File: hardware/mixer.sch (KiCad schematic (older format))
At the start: 31 parts, among them U26 5400BL15B050E, U27 5400BL15B050E, U28 5400BL15B050E, U29 ADL5802

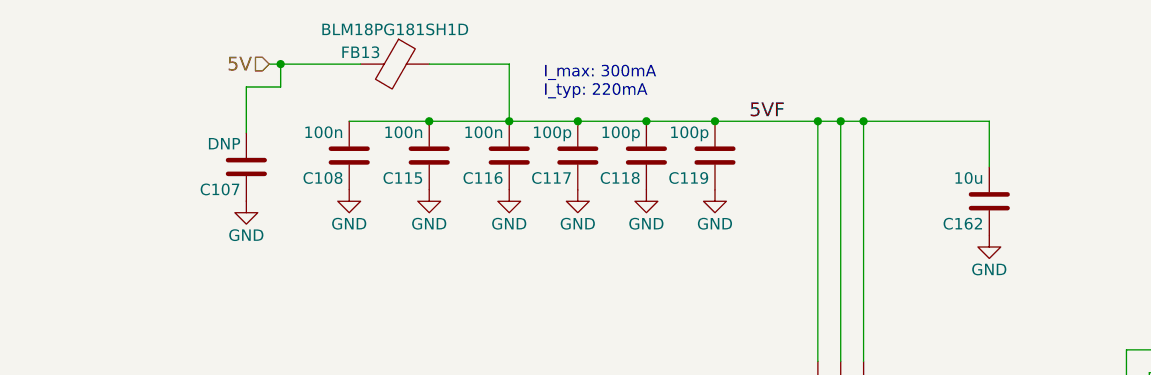
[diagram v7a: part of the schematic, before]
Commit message: Fixed ERC errors.
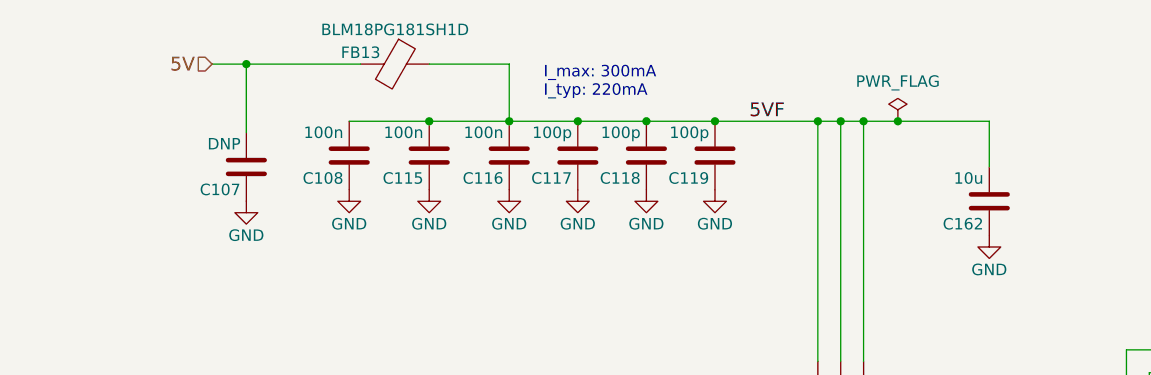
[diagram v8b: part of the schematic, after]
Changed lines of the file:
@@
 Text HLabel 8600 3450 2    60   Output ~ 0
 IF1-
-Text HLabel 3100 2200 0    60   Input ~ 0
-5V
 $Comp
 L fmcw-rescue:ADL5802-fmcw3-rescue U?
@@
 	1    0    0    -1
 $EndComp
-Wire Wire Line
-	3000 2500 3000 2300
-Wire Wire Line
-	3000 2300 3150 2300
-Wire Wire Line
-	3150 2300 3150 2200
-Wire Wire Line
-	3100 2200 3150 2200
-Connection ~ 3150 2200
 Connection ~ 4750 2450
 Text Label 5200 2450 0    60   ~ 0
@@
 	4750 2450 5050 2450
 Wire Wire Line
-	5700 2450 6250 2450
+	5700 2450 5850 2450
 Wire Wire Line
 	5250 5300 5350 5300
-Wire Wire Line
-	3150 2200 3500 2200
 Wire Wire Line
 	3800 2200 4150 2200
@@
 Wire Wire Line
 	950  4050 2100 4050
+Wire Wire Line
+	2850 2200 3000 2200
+Wire Wire Line
+	3000 2200 3000 2500
+Connection ~ 3000 2200
+Wire Wire Line
+	3000 2200 3500 2200
+$Comp
+L power:PWR_FLAG #FLG0110
+U 1 1 5CDA3D12
+P 5850 2450
+F 0 "#FLG0110" H 5850 2525 50  0001 C CNN
+F 1 "PWR_FLAG" H 5850 2624 50  0000 C CNN
+F 2 "" H 5850 2450 50  0001 C CNN
+F 3 "~" H 5850 2450 50  0001 C CNN
+	1    5850 2450
+	1    0    0    -1
+$EndComp
+Connection ~ 5850 2450
+Wire Wire Line
+	5850 2450 6250 2450
+Text HLabel 2850 2200 0    60   Input ~ 0
+5V
 $EndSCHEMATC
